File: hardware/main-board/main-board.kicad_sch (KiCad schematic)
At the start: 47 parts, among them J1 USB_C_Receptacle_USB2.0, J2 DNI, J3 Display Connector, U2 STM32L072KZT6, U4 USBLC6-2SC6, U5 TC1301A-APA

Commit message: Implement VSYNC reference signal
Adds a 32.768kHz oscillator and a binary counter to divide it, providing
a stable 128Hz signal routed to the sensor's VSYNC pin.
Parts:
- TP1, TP2: footprint TestPoint:TestPoint_Pad_D2.0mm -> TestPoint:TestPoint_Pad_D1.0mm
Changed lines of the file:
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@@
 			)
 		)
-		(property "Footprint" "TestPoint:TestPoint_Pad_D2.0mm"
+		(property "Footprint" "TestPoint:TestPoint_Pad_D1.0mm"
 			(at 75.565 114.935 0)
 			(effects
@@
 			)
 		)
+		(property "Manufacturer" ""
+			(at 70.485 114.935 0)
+			(effects
+				(font
+					(size 1.27 1.27)
+				)
+				(hide yes)
+			)
+		)
+		(property "Manufacturer PN" ""
+			(at 70.485 114.935 0)
+			(effects
+				(font
+					(size 1.27 1.27)
+				)
+				(hide yes)
+			)
+		)
+		(property "Supplier" ""
+			(at 70.485 114.935 0)
+			(effects
+				(font
+					(size 1.27 1.27)
+				)
+				(hide yes)
+			)
+		)
+		(property "Supplier PN" ""
+			(at 70.485 114.935 0)
+			(effects
+				(font
+					(size 1.27 1.27)
+				)
+				(hide yes)
+			)
+		)
 		(pin "1"
 		)
@@
 			)
 		)
-		(property "Footprint" "TestPoint:TestPoint_Pad_D2.0mm"
+		(property "Footprint" "TestPoint:TestPoint_Pad_D1.0mm"
 			(at 86.995 114.935 0)
 			(effects
@@
 			(at 81.915 114.935 0)
 			(effects
+				(font
+					(size 1.27 1.27)
+				)
+				(hide yes)
+			)
+		)
+		(property "Manufacturer" ""
+			(at 81.915 114.935 0)
+			(effects
+				(font
+					(size 1.27 1.27)
+				)
+				(hide yes)
+			)
+		)
+		(property "Manufacturer PN" ""
+			(at 81.915 114.935 0)
+			(effects
+				(font
+					(size 1.27 1.27)
+				)
+				(hide yes)
+			)
+		)
+		(property "Supplier" ""
+			(at 81.915 114.935 0)
+			(effects
+				(font
+					(size 1.27 1.27)
+				)
+				(hide yes)
+			)
+		)
+		(property "Supplier PN" ""
+			(at 81.915 114.935 0)
+			(effects

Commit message: Final tweaks for Rev C manufacture
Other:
- moved on the sheet: D7, D8, J2

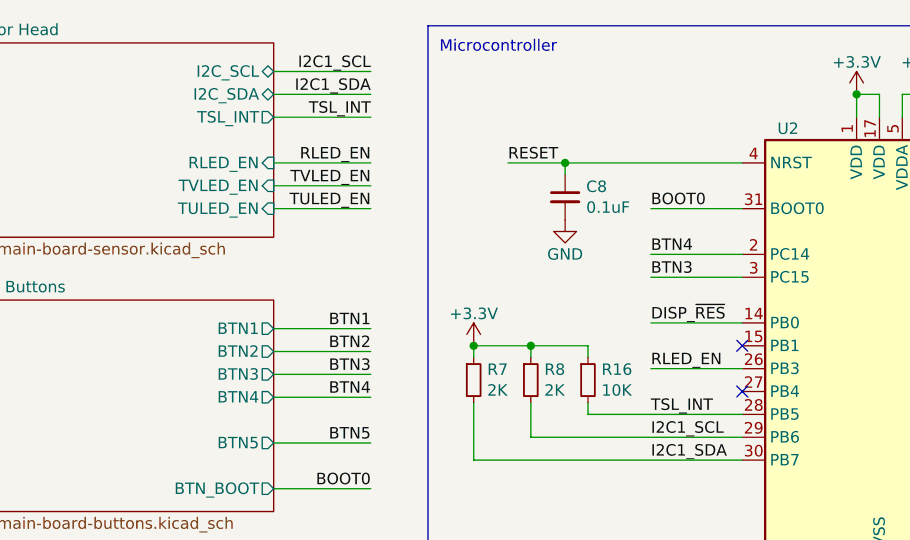
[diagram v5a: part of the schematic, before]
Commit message: Fix net name for reflection LEDs
This should match the identifer used in the firmware, for consistency
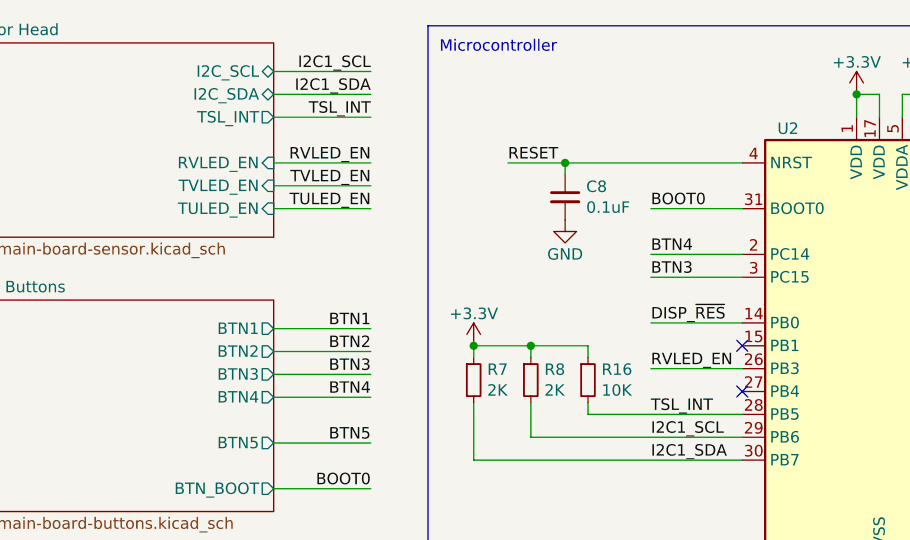
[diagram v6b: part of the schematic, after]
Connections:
- net RLED_EN renamed RVLED_EN
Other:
- sheet Sensor Head ports: added RVLED_EN; removed RLED_EN
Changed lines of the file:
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@@
 		)
 	)
-	(label "RLED_EN"
+	(label "RVLED_EN"
 		(at 91.44 52.705 0)
 		(fields_autoplaced yes)
@@
 		)
 	)
-	(label "RLED_EN"
+	(label "RVLED_EN"
 		(at 60.325 29.845 180)
 		(fields_autoplaced yes)
@@
 			)
 		)
-		(pin "RLED_EN" input
+		(pin "RVLED_EN" input
 			(at 49.53 29.845 0)
 			(effects

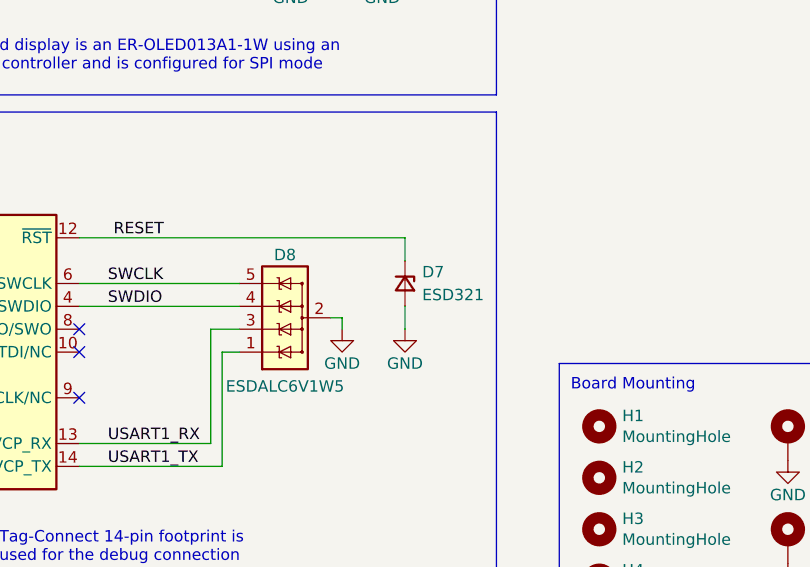
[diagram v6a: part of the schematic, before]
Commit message: Update ESD321 symbols and footprints
Correct the library symbols and footprints used for the ESD321DYAR so
that the reversed pin 1 indiciation of these components still gets
assembled correctly.

Keeping the existing diode footprint with its marking, and adding a
supplemental dot to indicate how pin 1 differs from what this footprint
otherwise suggests.

This should make all the data correct, though an extra note in assembly
guidance will be necessary just in case.

Fix #1
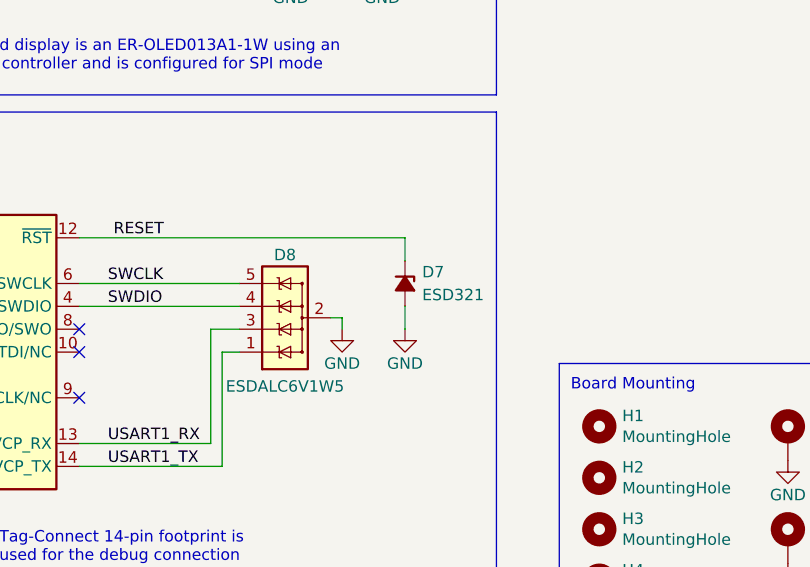
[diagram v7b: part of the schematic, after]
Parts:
- D7: symbol Device:D_Zener_Small -> Project:ESD321DYAR
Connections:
- net GND: now also D7.1 (A); no longer D7.2 (A)
- net RESET: now also D7.2 (K); no longer D7.1 (K)
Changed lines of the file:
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@@
 	(title_block
 		(title "Printalyzer UV/VIS Densitometer - Main Board")
-		(date "2024-09-24")
+		(date "2024-10-24")
 		(rev "C")
 		(company "Dektronics, Inc.")
@@
 	)
 	(symbol
-		(lib_id "Device:D_Zener_Small")
+		(lib_id "Project:ESD321DYAR")
 		(at 201.295 116.205 270)
 		(unit 1)
@@
 		)
 		(property "Footprint" "lib_fp:D_TI_SOD-523_DYA0002A"
-			(at 201.295 116.205 90)
+			(at 193.421 116.205 0)
 			(effects
 				(font
@@
 		)
 		(property "Datasheet" "https://www.ti.com/lit/ds/symlink/esd321.pdf"
-			(at 201.295 116.205 90)
+			(at 190.881 116.205 0)
 			(effects
 				(font
@@
 		)
 		(property "Description" "TVS DIODE 3.6VWM 6.3VC SOD523"
-			(at 201.295 116.205 0)
+			(at 195.961 116.205 0)
 			(effects
 				(font

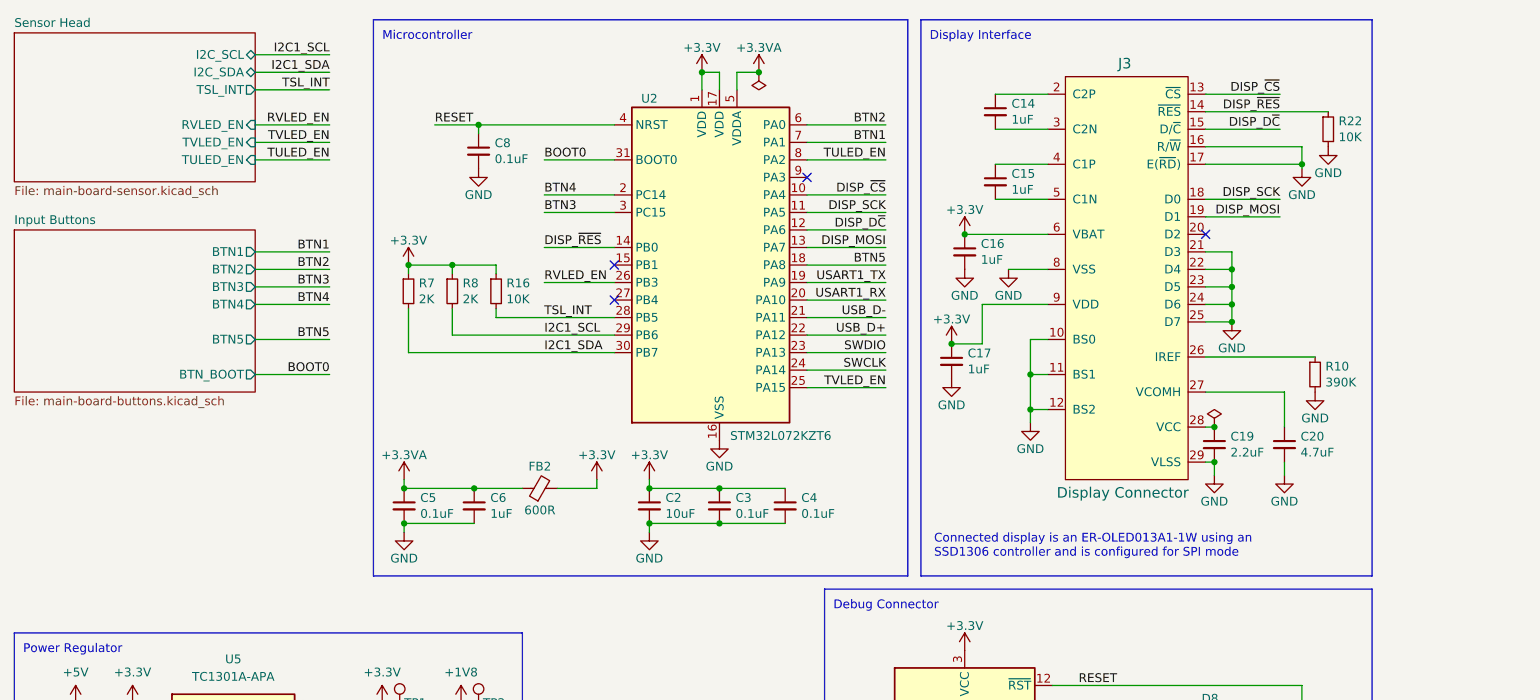
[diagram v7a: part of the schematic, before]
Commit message: Remove crystal reference and reroute VSYNC pin
In testing with Rev C hardware, it was determined that using the VSYNC
pin to calibrate the TSL2585's internal oscillator can actually
introduce more instability in sensor timing than would otherwise exist.
Furthermore, the most likely factor affecting oscillator stability is
temperature, which we're already planning to correct for.

Thus these extra components should be removed from the design.

For the sake of future-proofing, the VSYNC pin is now rounded directly
to the MCU (though a pull-up resistor), in case someday it is decided to
use this as a measurement trigger. It is also likely this pin will never
be used, but it doesn't really hurt to do this.

Fix #2
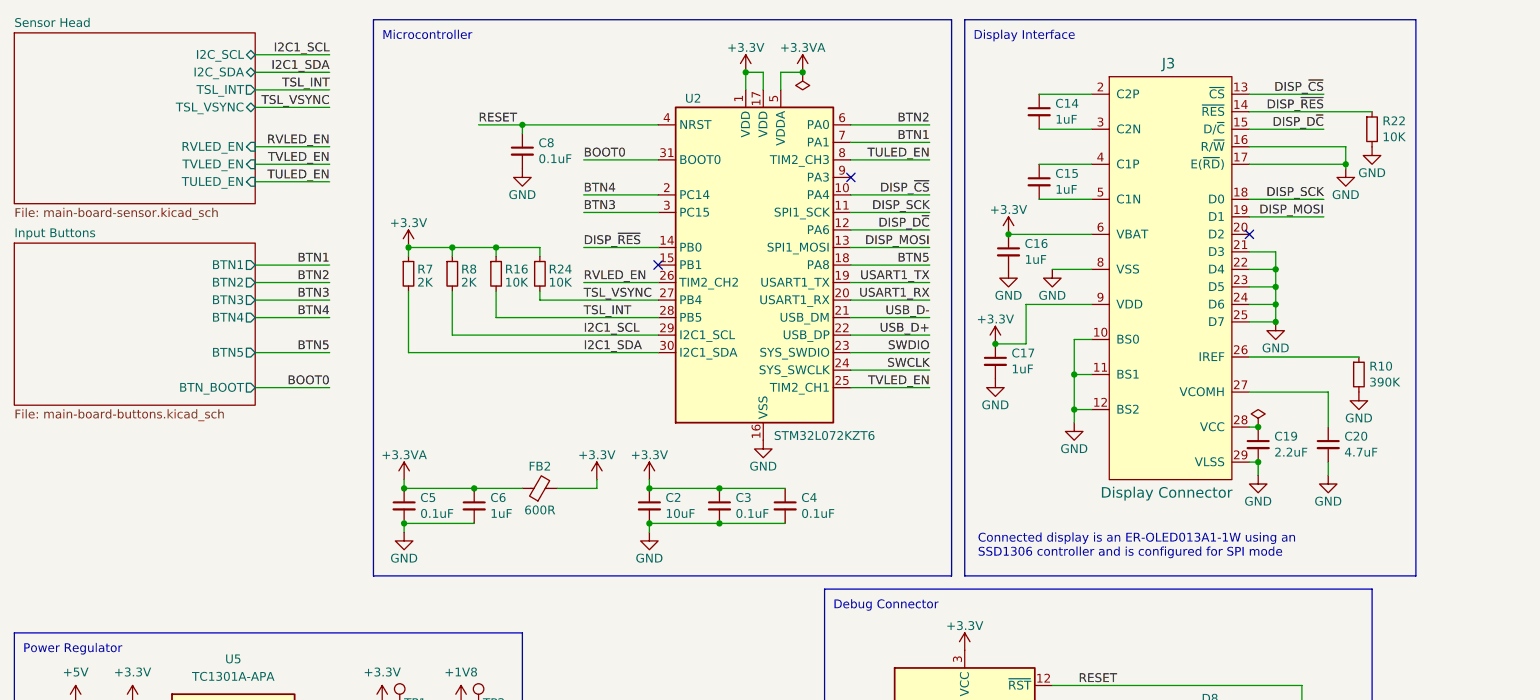
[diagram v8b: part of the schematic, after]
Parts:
- added R24: 10K, Resistor_SMD:R_0603_1608Metric, symbol Device:R_Small
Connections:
- net +3.3V: now also R24.1
- net TSL_VSYNC: now reaches U2.27 (PB4)
- net TSL_VSYNC: now also R24.2
- no-connect marks 11 -> 10
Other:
- sheet Sensor Head ports: added TSL_VSYNC; removed none
- moved on the sheet: C14, C15, C16, C17, C19, C20, C8, J3, R10, R16, R22, R7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
